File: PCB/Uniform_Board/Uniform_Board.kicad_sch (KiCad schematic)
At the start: 159 parts, among them U1 STM32L072KZT6, U2 SN74AHCT1G125DBVR

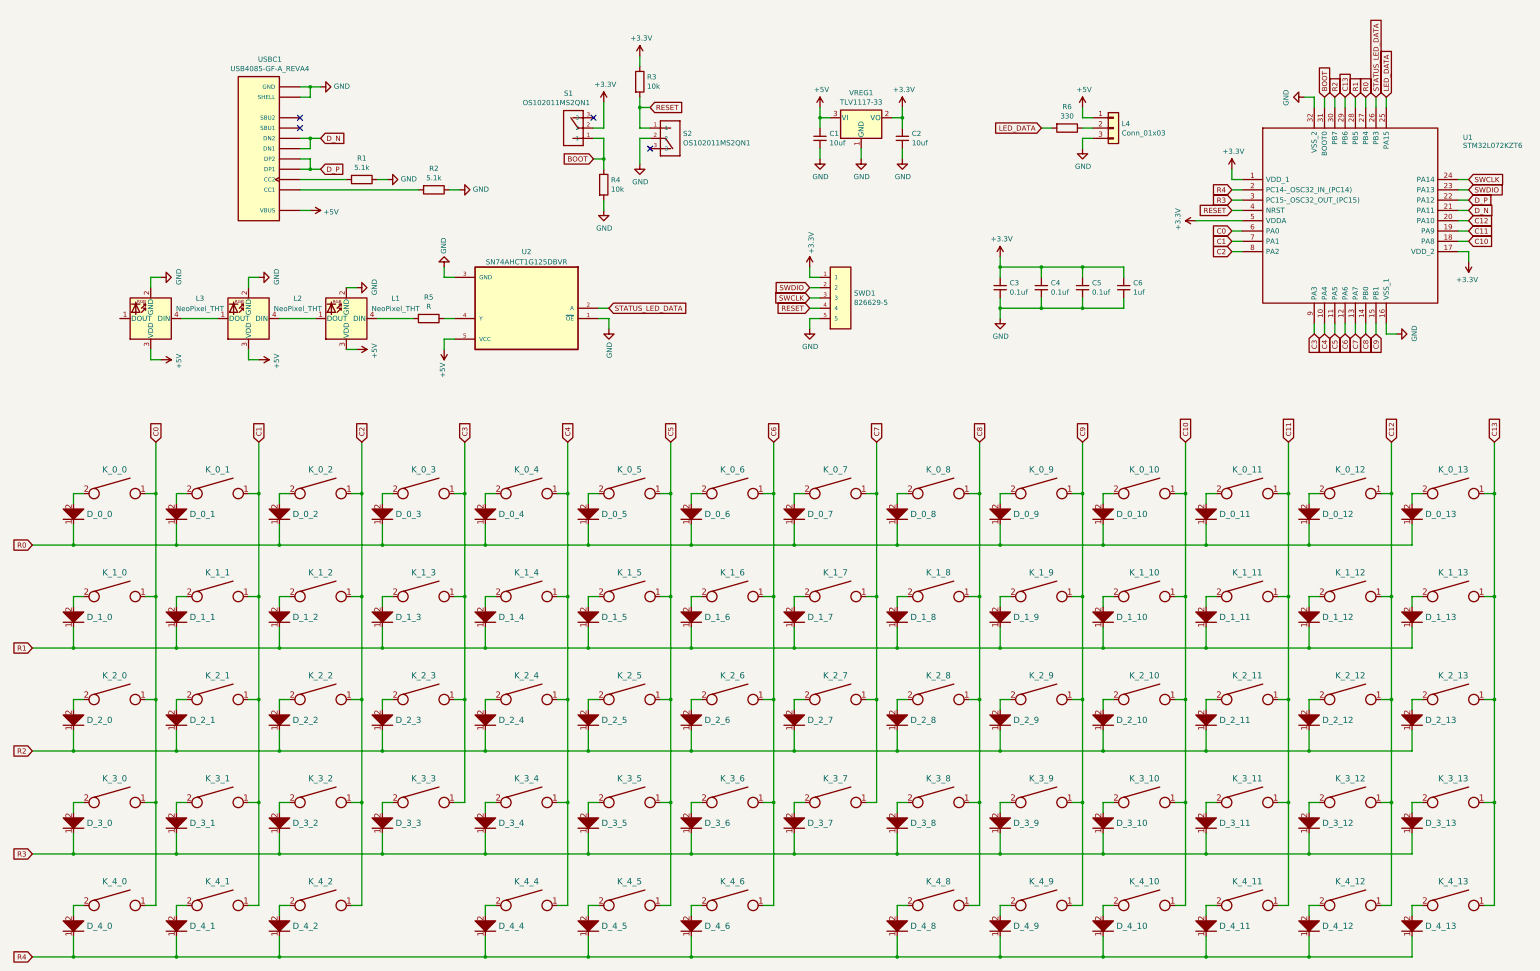
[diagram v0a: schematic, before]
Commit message: broke Uniform into two projects - uniform_board and uniform_module. Finished uniform_module schematic
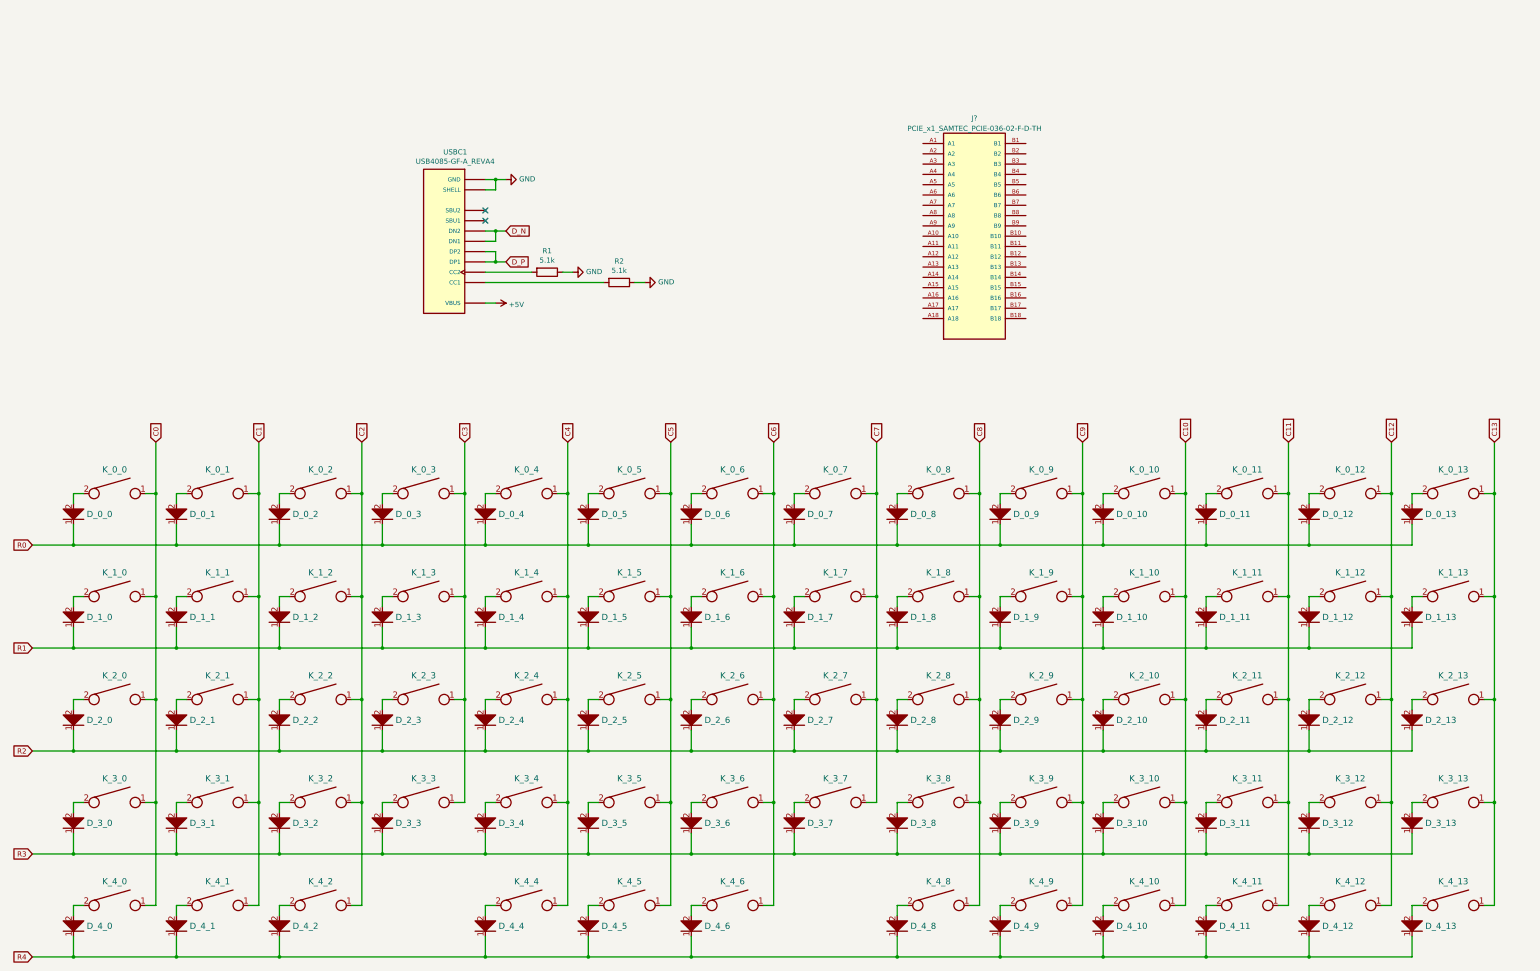
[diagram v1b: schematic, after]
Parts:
- removed C1, C2: 10uf, ul_FG16X7R1E106KRT06:FG16X7R1E106KRT06, symbol Device:C_Small
- removed C3, C4, C5: 0.1uf, Resistor_THT:R_Axial_DIN0207_L6.3mm_D2.5mm_P7.62mm_Horizontal, symbol Device:C_Small
- removed C6: 1uf, RDER71H105K2M1H03A:CAP_RDER71H105K2M1H03A, symbol Device:C_Small
- removed L1, L2, L3: NeoPixel_THT, Neopixel:LED_D5.0mm-4_RGB, symbol LED:NeoPixel_THT
- removed L4: Conn_01x03, Connector_PinHeader_2.54mm:PinHeader_1x03_P2.54mm_Vertical, symbol Connector_Generic:Conn_01x03
- removed R3, R4: 10k, Resistor_THT:R_Axial_DIN0204_L3.6mm_D1.6mm_P7.62mm_Horizontal, symbol Device:R
- removed R5: R, Resistor_THT:R_Axial_DIN0309_L9.0mm_D3.2mm_P12.70mm_Horizontal, symbol Device:R
- removed R6: 330, Resistor_THT:R_Axial_DIN0309_L9.0mm_D3.2mm_P12.70mm_Horizontal, symbol Device:R
- removed S1, S2: OS102011MS2QN1, OS102011MS2QN1:SW_OS102011MS2QN1, symbol OS102011MS2QN1:OS102011MS2QN1
- removed SWD1: 826629-5, 826629-5:TE_826629-5, symbol 826629-5:826629-5
- removed U1: STM32L072KZT6, STM32L072KZT6:QFP80P900X900X160-32N, symbol STM32L072KZT6:STM32L072KZT6
- removed U2: SN74AHCT1G125DBVR, SN74AHCT1G125DBVR:SOT95P280X145-5N, symbol SN74AHCT1G125DBVR:SN74AHCT1G125DBVR
- removed VREG1: TLV1117-33, TLV1117-33IDCY:SOT230P700X180-4N, symbol Regulator_Linear:TLV1117-33
- added J?: PCIE_x1_SAMTEC_PCIE-036-02-F-D-TH, PCIE-036-02-F-D-TH:SAMTEC_PCIE-036-02-F-D-TH, symbol Uniform:PCIE_x1_SAMTEC_PCIE-036-02-F-D-TH
- USBC1: footprint USB4085-GF-A_REVA4:GCT_USB4085-GF-A_REVA4 -> GCT_USB4085-GF-A_REVA4; symbol USB4085-GF-A_REVA4:USB4085-GF-A_REVA4 -> Uniform:USBC_USB4085-GF-A_REVA4
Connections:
- no-connect marks 4 -> 2
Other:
- moved on the sheet: R1, R2, USBC1

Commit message: completed uniform_board schematic
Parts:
- gave numbers to parts that had none: 1
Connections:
- net +5V: now also J1.A1
- net C0: now also J1.A10
- net C1: now also J1.A11
- net C10: now also J1.B5
- net C11: now also J1.B6
- net C12: now also J1.B7
- net C13: now also J1.B8
- net C2: now also J1.A12
- net C3: now also J1.A13
- net C4: now also J1.A14
- net C5: now also J1.A15
- net C6: now also J1.A16
- net C7: now also J1.A17
- net C8: now also J1.B3
- net C9: now also J1.B4
- net D_N: now also J1.A4
- net D_P: now also J1.A3
- net GND: now also J1.A2, J1.B2
- net R0: now also J1.A5
- net R1: now also J1.A6
- net R2: now also J1.A7
- net R3: now also J1.A8
- net R4: now also J1.A9
- no-connect marks 2 -> 14
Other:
- moved on the sheet: J1, R1, R2, USBC1

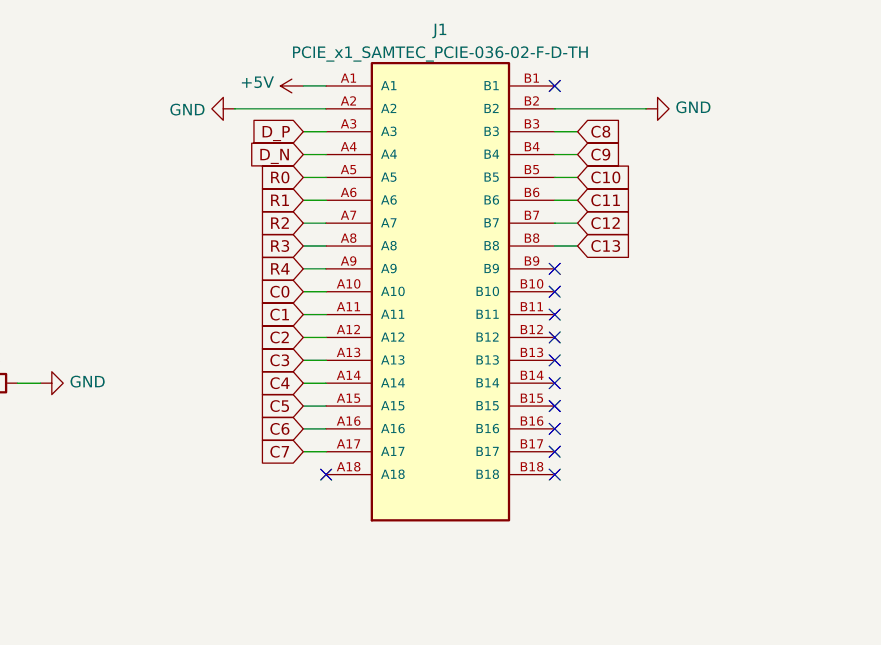
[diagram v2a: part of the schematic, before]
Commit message: board USBC and power routed to PCIE, pre row/column routing
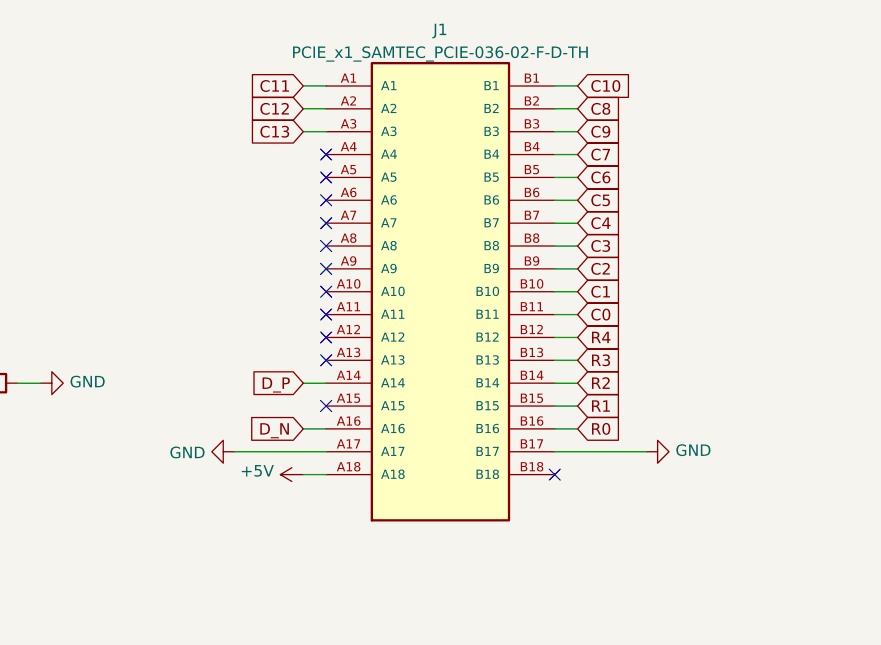
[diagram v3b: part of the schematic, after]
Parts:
- D_0_0, D_0_1, D_0_10, D_0_11, D_0_12, D_0_13, D_0_2, D_0_3, D_0_4, D_0_5, D_0_6, D_0_7, D_0_8, D_0_9, D_1_0, D_1_1, D_1_10, D_1_11, D_1_12, D_1_13, D_1_2, D_1_3, D_1_4, D_1_5, D_1_6, D_1_7, D_1_8, D_1_9, D_2_0, D_2_1, D_2_10, D_2_11, D_2_12, D_2_13, D_2_2, D_2_3, D_2_4, D_2_5, D_2_6, D_2_7, D_2_8, D_2_9, D_3_0, D_3_1, D_3_10, D_3_11, D_3_12, D_3_13, D_3_2, D_3_3, D_3_4, D_3_5, D_3_6, D_3_7, D_3_8, D_3_9, D_4_0, D_4_1, D_4_10, D_4_11, D_4_12, D_4_13, D_4_2, D_4_4, D_4_5, D_4_6, D_4_8, D_4_9: footprint 1N4148:DIOAD829W49L456D191 -> Uniform:Diode_DIOAD829W49L456D191
- J1: footprint PCIE-036-02-F-D-TH:SAMTEC_PCIE-036-02-F-D-TH -> Uniform:SAMTEC_PCIE-036-02-F-D-TH
- R1, R2: footprint Resistor_THT:R_Axial_DIN0204_L3.6mm_D1.6mm_P7.62mm_Horizontal -> Resistor_SMD:R_0603_1608Metric_Pad0.98x0.95mm_HandSolder
- USBC1: footprint GCT_USB4085-GF-A_REVA4 -> Uniform:USBC_USB4085-GF-A
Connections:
- net +5V: now also J1.A18; no longer J1.A1
- net C0: now also J1.B11; no longer J1.A10
- net C1: now also J1.B10; no longer J1.A11
- net C10: now also J1.B1; no longer J1.B5
- net C11: now also J1.A1; no longer J1.B6
- net C12: now also J1.A2; no longer J1.B7
- net C13: now also J1.A3; no longer J1.B8
- net C2: now also J1.B9; no longer J1.A12
- net C3: now also J1.B8; no longer J1.A13
- net C4: now also J1.B7; no longer J1.A14
- net C5: now also J1.B6; no longer J1.A15
- net C6: now also J1.B5; no longer J1.A16
- net C7: now also J1.B4; no longer J1.A17
- net C8: now also J1.B2; no longer J1.B3
- net C9: now also J1.B3; no longer J1.B4
- net D_N: now also J1.A16; no longer J1.A4
- net D_P: now also J1.A14; no longer J1.A3
- net GND: now also J1.A17, J1.B17; no longer J1.A2, J1.B2
- net R0: now also J1.B16; no longer J1.A5
- net R1: now also J1.B15; no longer J1.A6
- net R2: now also J1.B14; no longer J1.A7
- net R3: now also J1.B13; no longer J1.A8
- net R4: now also J1.B12; no longer J1.A9

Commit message: started board routing; first attempt
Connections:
- net C0: now also J1.A3; no longer J1.B11
- net C1: now also J1.A2; no longer J1.B10
- net C10: now also J1.B8; no longer J1.B1
- net C11: now also J1.B9; no longer J1.A1
- net C12: now also J1.B10; no longer J1.A2
- net C13: now also J1.B11; no longer J1.A3
- net C2: now also J1.A1; no longer J1.B9
- net C3: now also J1.B1; no longer J1.B8
- net C4: now also J1.B2; no longer J1.B7
- net C5: now also J1.B3; no longer J1.B6
- net C6: now also J1.B4; no longer J1.B5
- net C7: now also J1.B5; no longer J1.B4
- net C8: now also J1.B6; no longer J1.B2
- net C9: now also J1.B7; no longer J1.B3

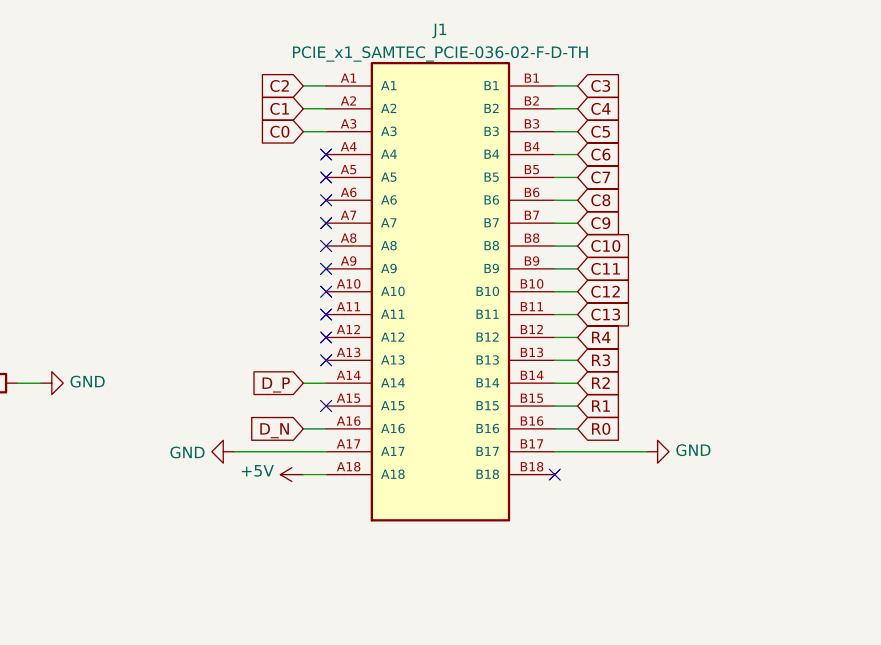
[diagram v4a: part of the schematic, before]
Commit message: PCIE Edge Connector footprint dimmensions and edge cuts done
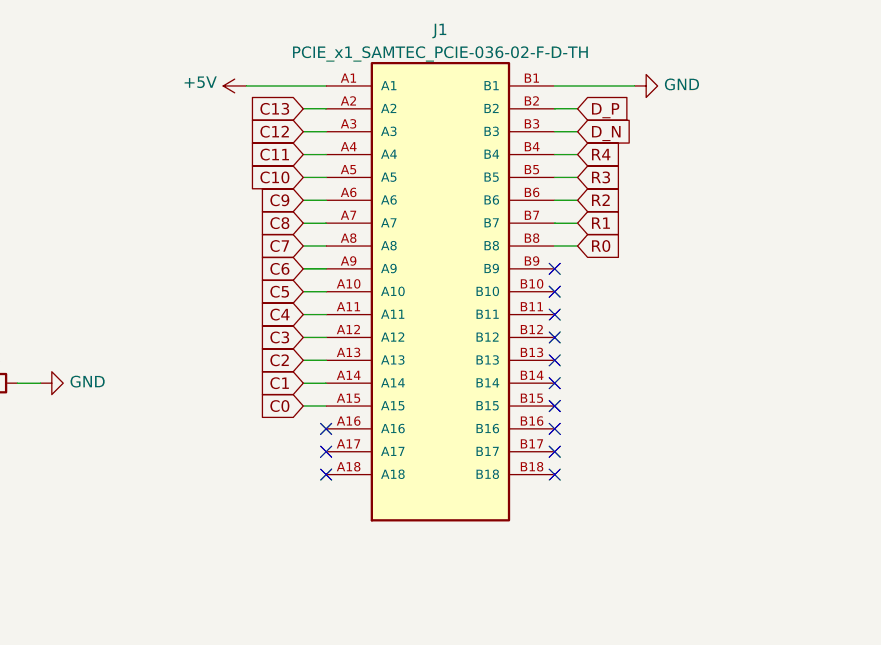
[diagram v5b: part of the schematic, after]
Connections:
- net +5V: now also J1.A1; no longer J1.A18
- net C0: now also J1.A15; no longer J1.A3
- net C1: now also J1.A14; no longer J1.A2
- net C10: now also J1.A5; no longer J1.B8
- net C11: now also J1.A4; no longer J1.B9
- net C12: now also J1.A3; no longer J1.B10
- net C13: now also J1.A2; no longer J1.B11
- net C2: now also J1.A13; no longer J1.A1
- net C3: now also J1.A12; no longer J1.B1
- net C4: now also J1.A11; no longer J1.B2
- net C5: now also J1.A10; no longer J1.B3
- net C6: now also J1.A9; no longer J1.B4
- net C7: now also J1.A8; no longer J1.B5
- net C8: now also J1.A7; no longer J1.B6
- net C9: now also J1.A6; no longer J1.B7
- net D_N: now also J1.B3; no longer J1.A16
- net D_P: now also J1.B2; no longer J1.A14
- net GND: now also J1.B1; no longer J1.A17, J1.B17
- net R0: now also J1.B8; no longer J1.B16
- net R1: now also J1.B7; no longer J1.B15
- net R2: now also J1.B6; no longer J1.B14
- net R3: now also J1.B5; no longer J1.B13
- net R4: now also J1.B4; no longer J1.B12
- no-connect marks 14 -> 15

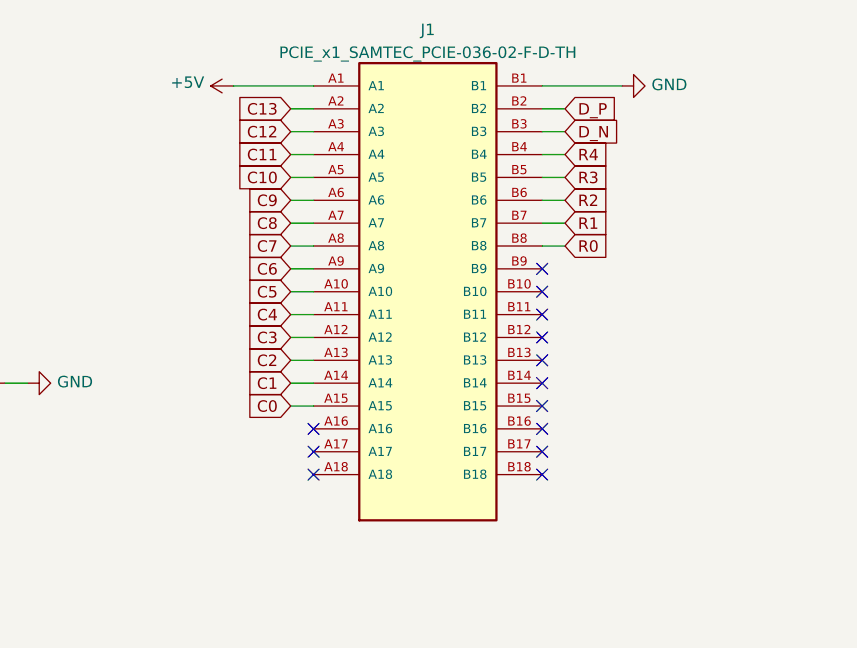
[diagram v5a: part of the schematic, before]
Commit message: improved trace origins on PCIE port/edge. Board rerouting done. Module rerouting in progress
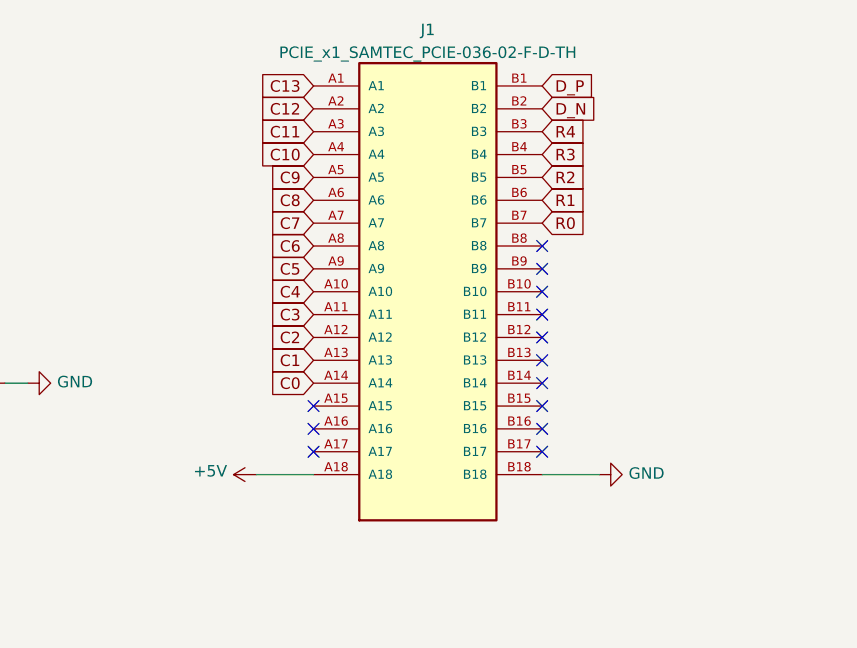
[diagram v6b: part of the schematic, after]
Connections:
- net +5V: now also J1.A18; no longer J1.A1
- net C0: now also J1.A14; no longer J1.A15
- net C1: now also J1.A13; no longer J1.A14
- net C10: now also J1.A4; no longer J1.A5
- net C11: now also J1.A3; no longer J1.A4
- net C12: now also J1.A2; no longer J1.A3
- net C13: now also J1.A1; no longer J1.A2
- net C2: now also J1.A12; no longer J1.A13
- net C3: now also J1.A11; no longer J1.A12
- net C4: now also J1.A10; no longer J1.A11
- net C5: now also J1.A9; no longer J1.A10
- net C6: now also J1.A8; no longer J1.A9
- net C7: now also J1.A7; no longer J1.A8
- net C8: now also J1.A6; no longer J1.A7
- net C9: now also J1.A5; no longer J1.A6
- net D_N: now also J1.B2; no longer J1.B3
- net D_P: now also J1.B1; no longer J1.B2
- net GND: now also J1.B18; no longer J1.B1
- net R0: now also J1.B7; no longer J1.B8
- net R1: now also J1.B6; no longer J1.B7
- net R2: now also J1.B5; no longer J1.B6
- net R3: now also J1.B4; no longer J1.B5
- net R4: now also J1.B3; no longer J1.B4
